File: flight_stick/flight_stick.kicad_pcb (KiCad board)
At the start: 2 copper layers, 66 parts, among them J1 Load Cell 1, J10 USB_C_Receptacle_USB2.0, J11 Conn_01x05_Pin, J3 Load Cell 5, J5 Load Cell 3, J7 Conn_01x04_Male, J8 Conn_01x05_Pin, J9 Conn_ST_STDC14, Q1 MMS8550, Q3 MMS8550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

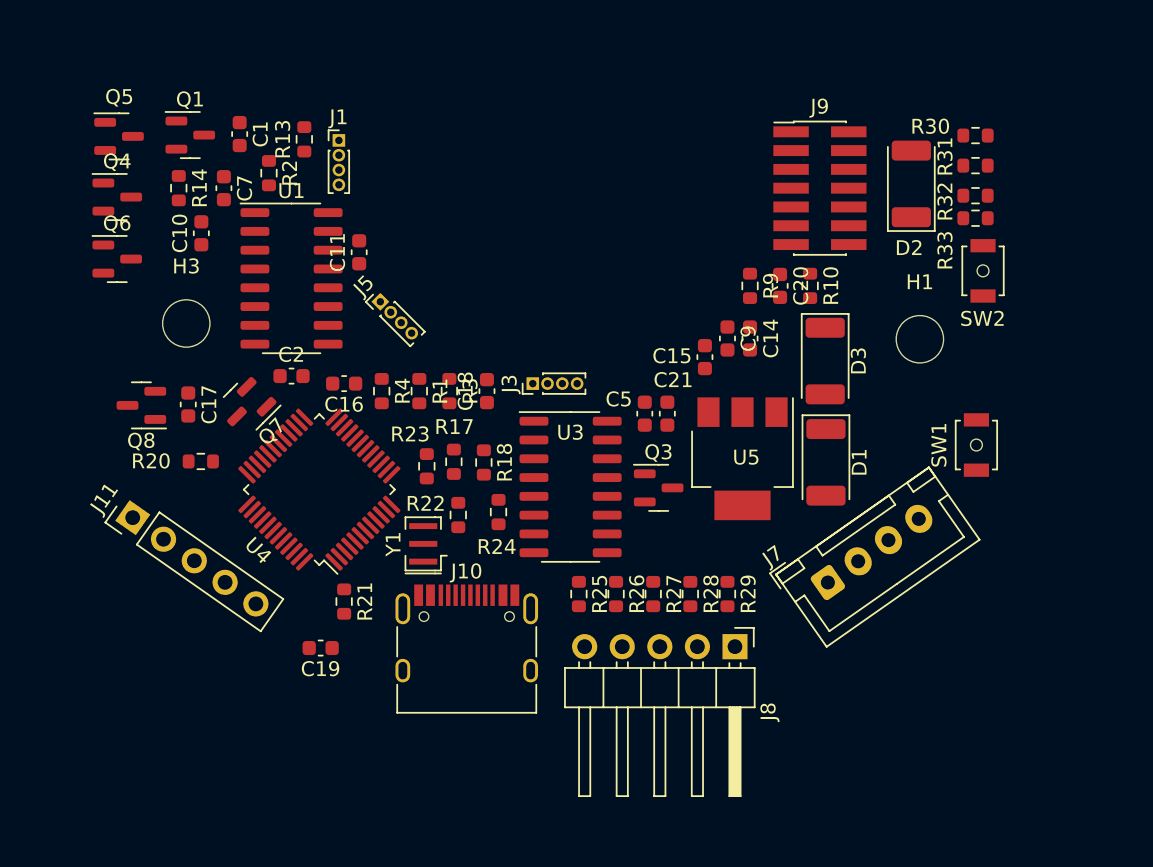
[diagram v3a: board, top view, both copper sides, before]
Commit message: Finalilzed Layout and began routing
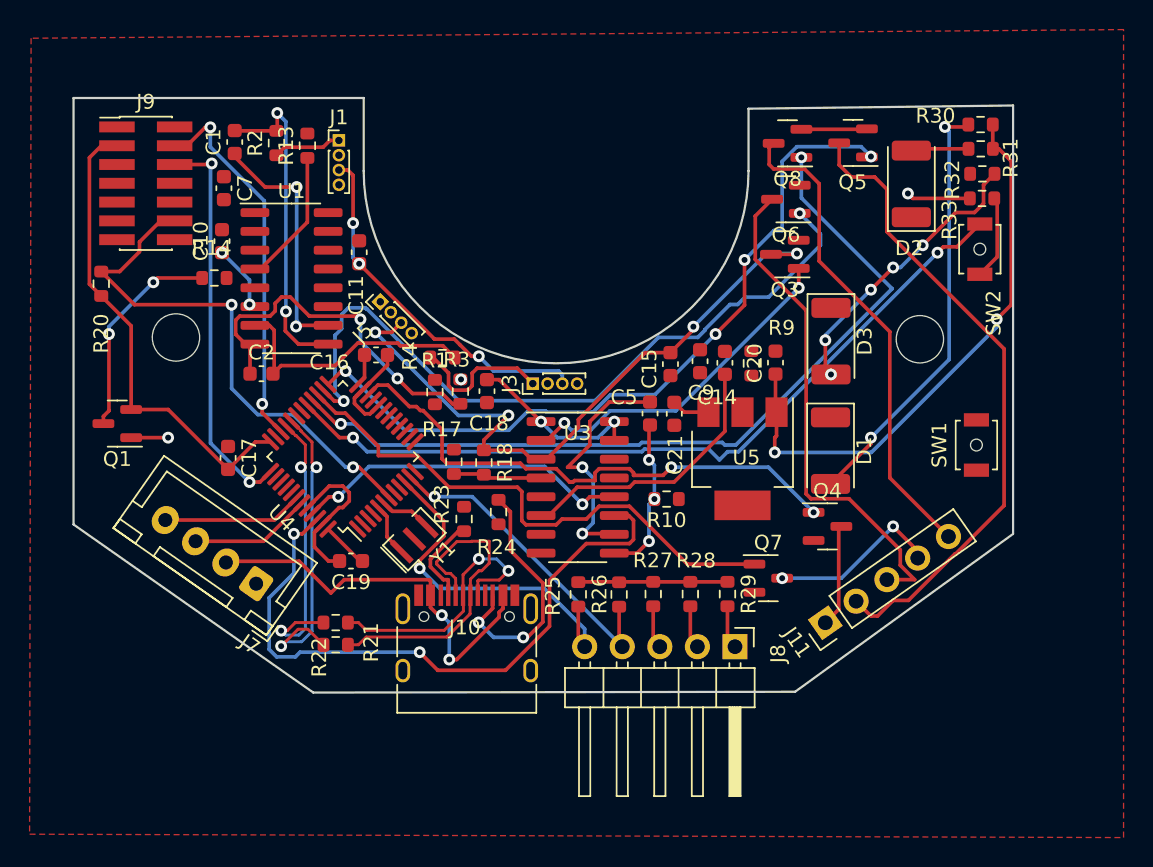
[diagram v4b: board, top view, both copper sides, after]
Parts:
- moved Q4 52.9 mm to (153.1, 127.0)
- moved Q5 49.6 mm to (154.8, 101.1), turned to 180 degrees
- moved J11 47.3 mm to (152.9, 133.5), turned to 125 degrees
- moved Q8 47.1 mm to (150.4, 101.1)
- moved J9 45.6 mm to (107.0, 103.8)
- moved Q6 45.4 mm to (150.3, 104.9), turned to 180 degrees
- moved J7 38.6 mm to (114.5, 130.9), turned to 145 degrees
- moved Q7 37.1 mm to (149.1, 130.5), turned to 0 degrees
- moved Q1 20.1 mm to (105.1, 120.0), turned to 180 degrees
- moved Q3 17.9 mm to (150.2, 108.6), turned to 180 degrees
- moved R10 17.4 mm to (142.2, 125.2), turned to 180 degrees
- moved R20 13.8 mm to (104.0, 110.6), turned to 90 degrees
- moved R22 11.0 mm to (119.8, 133.5), turned to 0 degrees
- moved R14 6.53 mm to (111.6, 110.2), turned to 0 degrees
- moved C19 6.23 mm to (120.9, 129.3)
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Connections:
- net Net-(J10-D+-PadA6) renamed /d+
- net Net-(J10-D--PadA7) renamed /d-
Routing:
- net +3.3V: track 0.00 -> 66.6 mm, vias 0 -> 3
- net +5V: track 0.00 -> 66.0 mm, vias 0 -> 4
- net /Trans5: track 0.00 -> 56.4 mm, vias 0 -> 2
- net Net-(U4-PA8): track 0.00 -> 53.7 mm, vias 0 -> 2
- net /Trans2: track 0.00 -> 51.8 mm, vias 0 -> 4
- net /Trans3: track 0.00 -> 50.3 mm, vias 0 -> 2
- net /E+_{LC3&4}: track 0.00 -> 45.8 mm, vias 0 -> 4
- net clk-yforce: track 0.00 -> 44.2 mm, vias 0 -> 2
- net Net-(J11-Pin_2): track 0.00 -> 43.6 mm
- net /E+_{LC1&2}: track 0.00 -> 39.1 mm, vias 0 -> 5
- net /Trans4: track 0.00 -> 36.8 mm
- net /Trans1: track 0.00 -> 36.7 mm, vias 0 -> 2
- net /mcureset: track 0.00 -> 35.9 mm, vias 0 -> 2
- net Net-(J11-Pin_3): track 0.00 -> 34.0 mm
- net Net-(J11-Pin_5): track 0.00 -> 32.9 mm
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- added copper zone on F.Cu, net GND
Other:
- board outline added: 63.5 x 40.2 mm

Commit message: Continued further routing
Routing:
- net /mcureset: track 35.9 -> 87.8 mm, vias 2 -> 8
- net +3.3V: track 66.6 -> 113.8 mm, vias 3 -> 6
- net /button4: track 2.93 -> 45.7 mm, vias 0 -> 4
- net /button3: track 2.92 -> 40.2 mm, vias 0 -> 8
- net /Programming_{RX}: track 0.00 -> 36.8 mm, vias 0 -> 4
- net +5V: track 66.0 -> 101.5 mm, vias 4 -> 6
- net /S+_{LC3}: track 0.00 -> 28.4 mm, vias 0 -> 1
- net /button5: track 2.94 -> 31.0 mm, vias 0 -> 3
- net /Programming_{TX}: track 0.00 -> 26.5 mm, vias 0 -> 4
- net Net-(Q1-B): track 2.50 -> 18.9 mm, vias 1 -> 4
- net Net-(U3-IN_{B+}): track 16.6 -> 24.8 mm, vias 2 -> 4
- net Net-(U4-PA8): track 53.7 -> 59.4 mm
- net /Trans5: track 56.4 -> 50.9 mm
- net GND: track 21.3 -> 26.3 mm
- net dout-yforce: track 23.0 -> 26.6 mm
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
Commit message: Added more routing, near complete
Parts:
- moved R32 16.6 mm to (156.0, 118.0), turned to 90 degrees
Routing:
- net GND: track 26.3 -> 99.5 mm, vias 0 -> 8
- net +3.3V: track 113.8 -> 162.8 mm, vias 6 -> 15
- net /button5: track 31.0 -> 51.2 mm, vias 3 -> 4
- net dout-xforce: track 0.00 -> 17.5 mm, vias 0 -> 2
- net Net-(D3-A): track 19.5 -> 2.88 mm, vias 5 -> 2
- net clk-xforce: track 0.00 -> 13.6 mm, vias 0 -> 2
- net /E+_{LC1&2}: track 39.1 -> 52.0 mm, vias 5 -> 7
- net /button3: track 40.2 -> 28.3 mm, vias 8 -> 6
- net Net-(Q1-B): track 18.9 -> 27.0 mm
- net Net-(U1-IN_{B-}): track 23.0 -> 28.5 mm
- net dout-yforce: track 26.6 -> 31.6 mm
- net /mcureset: track 87.8 -> 92.6 mm
- net Net-(J11-Pin_3): track 30.9 -> 33.3 mm
- net /codeio: track 26.0 -> 28.1 mm
- net Net-(U1-A_{FB}): track 11.4 -> 13.4 mm
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
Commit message: Completed Routing Draft
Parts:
- moved R1 17.4 mm to (116.8, 103.5), turned to 180 degrees
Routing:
- net GND: track 99.5 -> 257.1 mm, vias 8 -> 32
- net /S-_{LC3}: track 0.00 -> 77.0 mm, vias 0 -> 11
- net +3.3V: track 162.8 -> 219.8 mm, vias 15 -> 27
- net Net-(U4-PA7): track 0.00 -> 41.7 mm, vias 0 -> 2
- net /S+_{LC1}: track 0.00 -> 11.7 mm, vias 0 -> 1
- net dout-yforce: track 31.6 -> 41.4 mm
- net Net-(U3-IN_{B+}): track 24.8 -> 33.4 mm
- net Net-(U4-PA8): track 57.7 -> 65.9 mm
- net /mcureset: track 92.6 -> 100.1 mm
- net /S+_{LC2}: track 0.31 -> 7.49 mm, vias 1 -> 2
- net /Programming_{RX}: track 36.6 -> 42.3 mm
- net Net-(D1-A): track 29.2 -> 33.3 mm
- net /E+_{LC3&4}: track 46.1 -> 49.4 mm
- net clk-yforce: track 44.7 -> 47.9 mm
- net Net-(U3-IN_{B-}): track 10.9 -> 13.6 mm
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
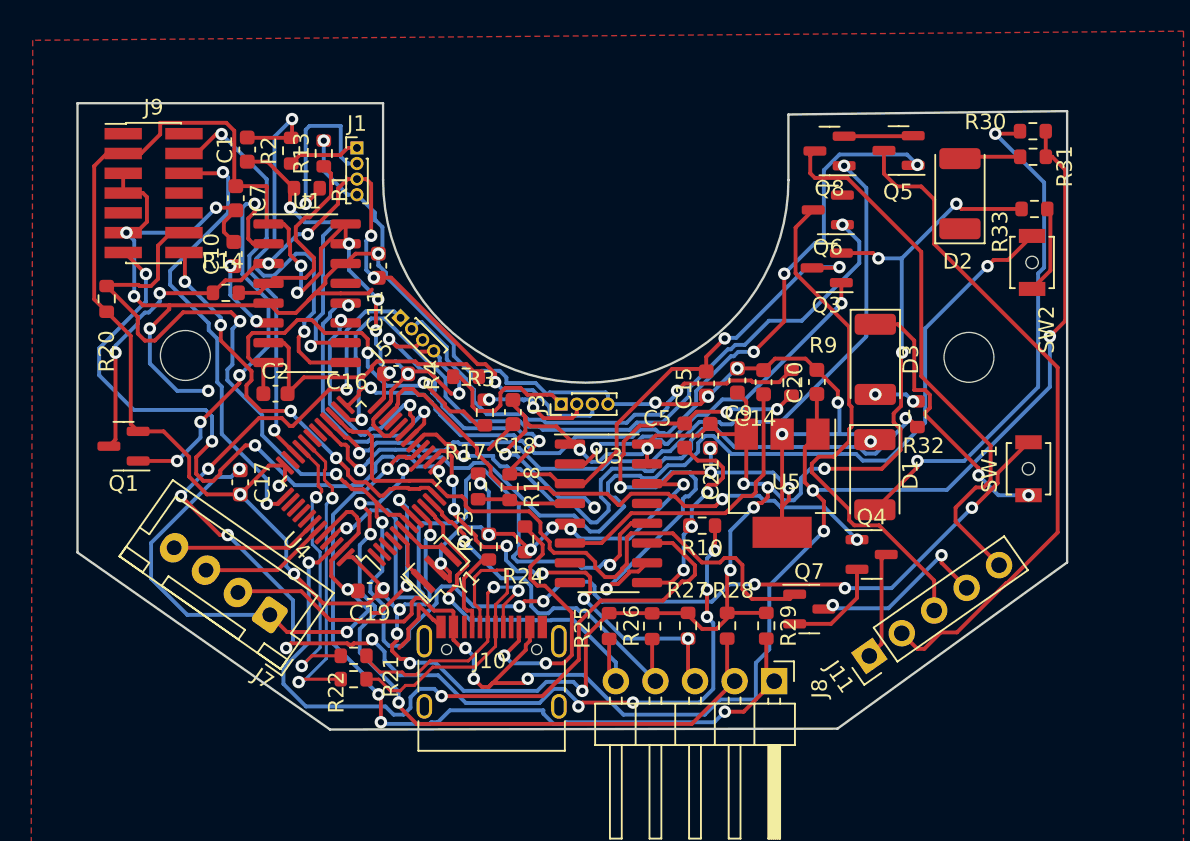
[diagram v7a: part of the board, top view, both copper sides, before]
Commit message: Completed Traces and Added Graphics
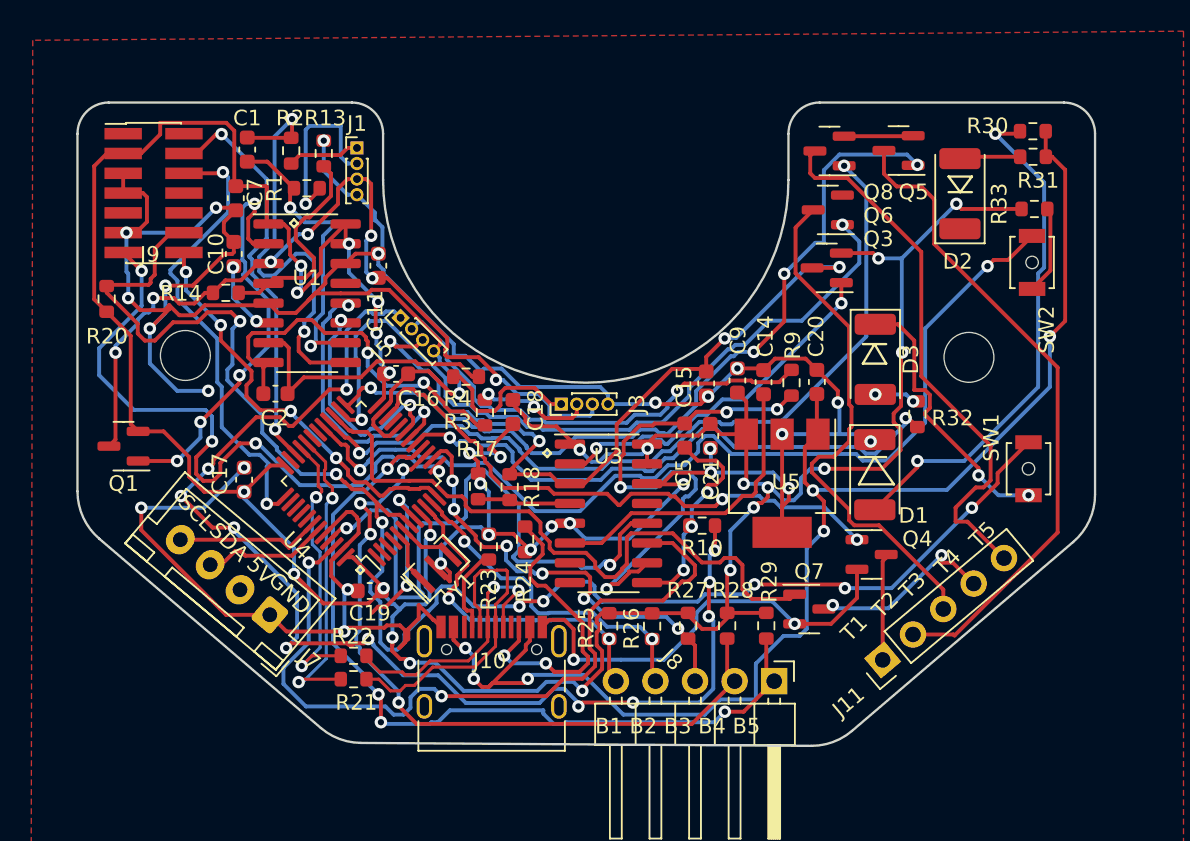
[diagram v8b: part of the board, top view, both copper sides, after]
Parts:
- moved J11 0.89 mm to (153.8, 133.8), turned to 130 degrees
- moved C17 0.30 mm to (112.8, 122.2)
- turned J7 to 140 degrees
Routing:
- net GND: track 257.1 -> 302.4 mm, vias 32 -> 37
- net +5V: track 103.9 -> 87.5 mm
- net +3.3V: track 219.8 -> 208.9 mm, vias 27 -> 23
- net Net-(U4-PA7): track 41.7 -> 37.7 mm
- net Net-(U4-PA8): track 65.9 -> 62.2 mm
- net /button1: track 24.0 -> 21.7 mm, vias 1 -> 2
- net Net-(J10-CC2): track 17.4 -> 19.7 mm
- net /button2: track 23.3 -> 22.0 mm, vias 1 -> 2
- net Net-(J11-Pin_2): track 43.6 -> 42.3 mm
- net /E+_{LC1&2}: track 54.0 -> 55.1 mm
- net clk-yforce: track 47.9 -> 49.1 mm
- net /S-_{LC3}: track 77.0 -> 77.7 mm
- net /button4: track 47.4 -> 46.8 mm
- net /E+_{LC3&4}: track 49.4 -> 48.9 mm
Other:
- board size 63.5 x 40.2 mm -> 65.3 x 41.3 mm
- board text added: "5V"
- board text added: "Aryan Ghosh :3"
- board text added: "B1 B2 B3 B4 B5"
- board text added: "Flightstick V3 HPVDT"
- board text added: "GND"
- board text added: "SCL"
- board text added: "SDA"
- board text added: "T1"
- board text added: "T2"
- board text added: "T3"
- board text added: "T4"
- board text added: "T5"
